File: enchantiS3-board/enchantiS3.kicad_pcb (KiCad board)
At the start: 4 copper layers, 55.9 x 25.4 mm, 59 parts, among them J1 USB_C_Receptacle_USB2.0, SW1 B3U-1000P, SW2 B3U-1000P, U1 USBLC6-2P6, U11 MAX17262REWL+T, U12 BQ25185DLHR, U13 ICM-42670-P, U2 MMC5633NJL, U4 NCP167AMX330TBG, U9 NCP167AMX330TBG

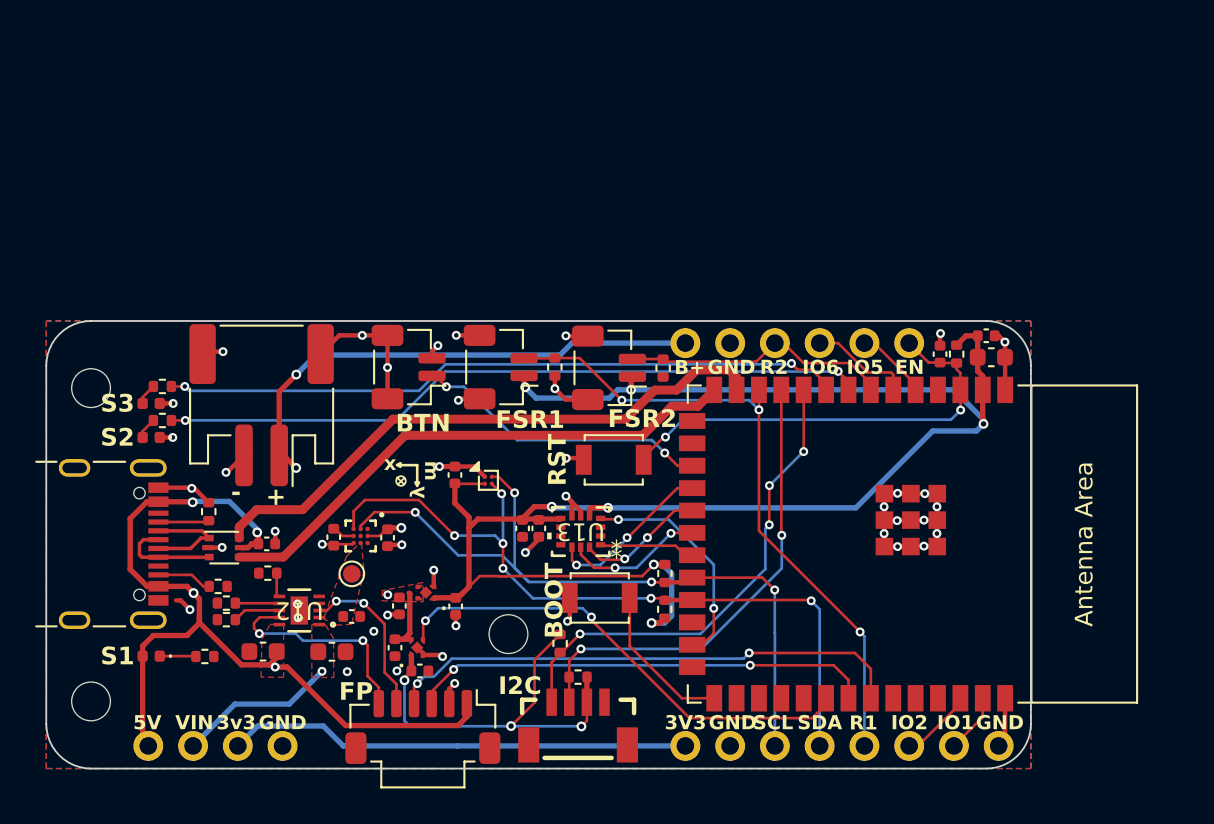
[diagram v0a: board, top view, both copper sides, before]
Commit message: revert tto two layer board, swap out magnetometer to mmc55983 and fuel gauge to MAX17260
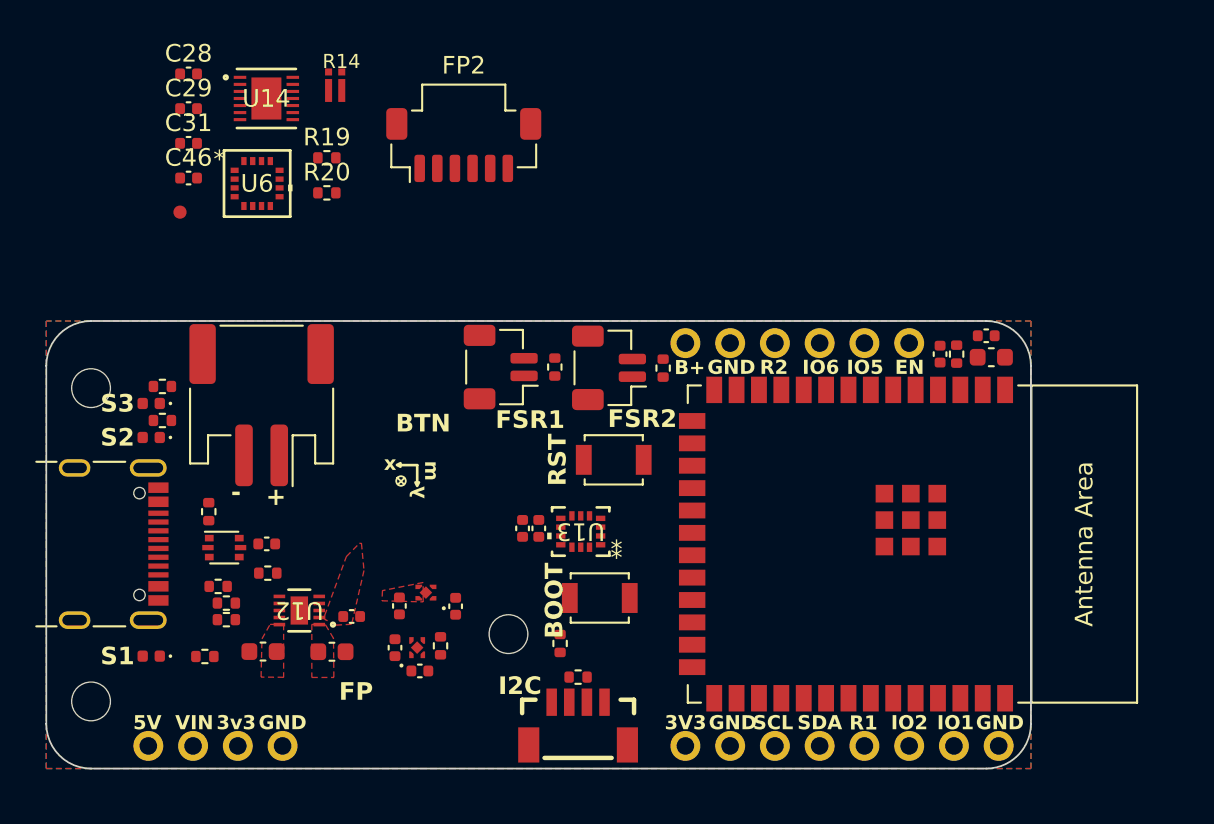
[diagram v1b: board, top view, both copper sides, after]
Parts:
- removed ANG2: CONN HEADER SMD 2POS 1MM, ENCHANTI_connectors:Molex_Pico-Clasp_2pin_Vertical
- removed C3: 220nF, Capacitor_SMD:C_0402_1005Metric
- removed C7: 0.1uF, Capacitor_SMD:C_0402_1005Metric
- removed C8: 0.47uF, Capacitor_SMD:C_0402_1005Metric
- removed FP1: CONN HEADER SMD 6POS 1MM, ENCHANTI_connectors:Molex_Pico-Clasp_501331-0607_1x06-1MP_P1.00mm_Vertical
- removed R4, R9: 2k2, Resistor_SMD:R_0402_1005Metric
- removed TP1: TestPoint, TestPoint:TestPoint_Pad_D1.0mm
- removed U11: MAX17262REWL+T, ENCHANTI_battery-management:MAX17262
- removed U2: MMC5633NJL, Package_BGA:WLP-4_0.86x0.86mm_P0.4mm
- added C28: 1uF, Capacitor_SMD:C_0402_1005Metric, F.Cu at (100.8, 34.2)
- added C29: 10uF, Capacitor_SMD:C_0402_1005Metric, F.Cu at (100.8, 36.2)
- added C31: 0.1uF, Capacitor_SMD:C_0402_1005Metric, F.Cu at (100.8, 38.2)
- added C46: 0.47uF, Capacitor_SMD:C_0402_1005Metric, F.Cu at (100.8, 40.1)
- added FP2: CONN HEADER SMD 6POS 1MM, Connector_Molex:Molex_Pico-Clasp_501331-0607_1x06-1MP_P1.00mm_Vertical, F.Cu at (116.4, 38.3)
- added R14: 1mOhm, ENCHANTI_resistors:L4CC0306, F.Cu at (109.1, 34.9)
- added R19: 2k2, Resistor_SMD:R_0402_1005Metric, F.Cu at (108.6, 39.0)
- added R20: 2k2, Resistor_SMD:R_0402_1005Metric, F.Cu at (108.6, 41.0)
- added R22: 100k, Resistor_SMD:R_0402_1005Metric, F.Cu at (115.1, 66.7)
- added TP4: TestPoint, SparkFun-Connector:TestPoint-0.75mm, F.Cu at (100.3, 42.1)
- added U14: MAX17260SETD+T, ENCHANTI_battery-management:TDFN-14-EP-ADI, F.Cu at (105.2, 35.6)
- added U6: MMC5983MA, ENCHANTI_MEMS:MMC5983MA_MEM, F.Cu at (104.7, 40.5)
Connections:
- ANG1 pad 1: +3V3 -> 3V3_AUX
- ANG3 pad 1: +3V3 -> 3V3_AUX
- C17 pad 1: +3V3 -> 3V3_AUX
- C18 pad 1: +3V3 -> 3V3_AUX
- U13 pad 5: +3V3 -> 3V3_AUX
- U13 pad 8: +3V3 -> 3V3_AUX
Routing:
- net +3V3: track 132.4 -> 0.00 mm, vias 7 -> 0
- net GND: track 65.2 -> 0.00 mm, vias 44 -> 0
- net VUSB: track 48.2 -> 0.00 mm, vias 4 -> 0
- net /SDA: track 42.6 -> 0.00 mm, vias 6 -> 0
- net /SCL: track 42.0 -> 0.00 mm, vias 4 -> 0
- net /BLUELED: track 40.3 -> 0.00 mm, vias 2 -> 0
- net /ORANGELED: track 38.7 -> 0.00 mm, vias 2 -> 0
- net /FSR1: track 37.2 -> 0.00 mm, vias 3 -> 0
- net /USBD-: track 33.4 -> 0.00 mm
- net +BATT: track 31.2 -> 0.00 mm, vias 3 -> 0
- net /USBD+: track 30.9 -> 0.00 mm
- net /LED2: track 29.7 -> 0.00 mm, vias 2 -> 0
- net /SCL2: track 27.7 -> 0.00 mm, vias 4 -> 0
- net /LDO_EN: track 27.6 -> 0.00 mm, vias 2 -> 0
- net /SDA2: track 26.7 -> 0.00 mm, vias 2 -> 0
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- removed copper zone on In2.Cu, net +3V3
- removed copper zone on In2.Cu, net +BATT
- removed copper zone on In1.Cu, net GND
- removed copper zone on In2.Cu, net GND
- removed copper zone on In2.Cu, net SYS
- removed copper zone on In2.Cu, net VUSB
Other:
- copper layers 4 -> 2
- rule pad_to_mask_clearance: 0.0508 -> 0
- board text removed: "1.8V"
- board text removed: "2 pin JST-PH Vertical Header"
- board text removed: "2 pin JST-SH Vertical Header"
- board text removed: "3.3V"
- board text removed: "4 pin JST-SH Vertical Header"
- board text removed: "BAT+"
- board text removed: "Boot Button"
- board text removed: "ESP32-S3 WROOM 2"
- board text removed: "Fuel Gauge"
- board text removed: "ICM20948"
- board text removed: "Indicator LEDs (RED)"
- board text removed: "MCP73871"
- board text removed: "NCP167AMX 180TBG"
- board text removed: "NCP167AMX 330TBG"
- board text removed: "Neopixel"
- board text removed: "Ohmite LVK12 Shunt Resistor"
- board text removed: "Reset Button"
- board text removed: "SYS"
- board text removed: "USB C Receptacle"
- board text removed: "USBLC6-LP6"

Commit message: Switched to using multi sheet schematic, added NPM1300 to handle power management and WiFi, finished initial PCB layout and routing
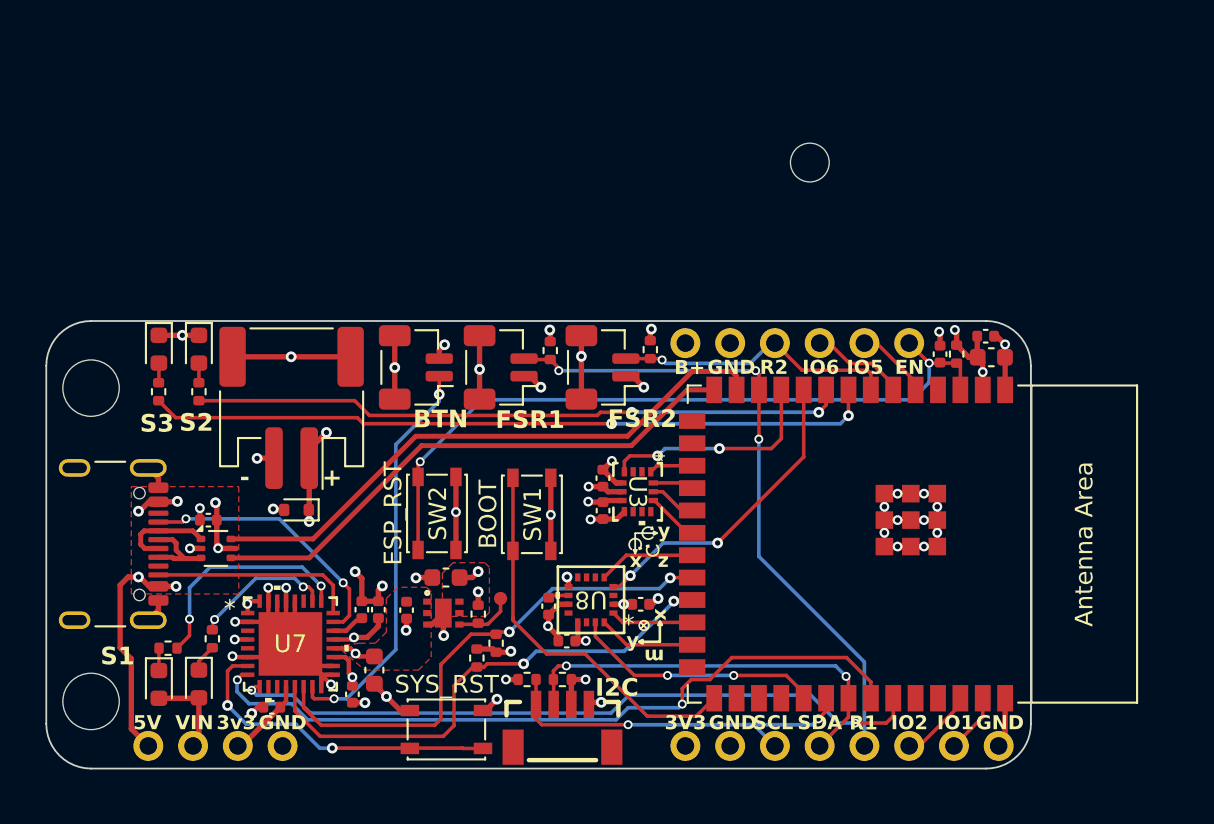
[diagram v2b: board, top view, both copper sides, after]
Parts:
- removed BT1: JST-PH-1x02-2.000mm, Connector_JST:JST_PH_S2B-PH-SM4-TB_1x02-1MP_P2.00mm_Horizontal
- removed C12, C17, C22, C28: 1uF, Capacitor_SMD:C_0402_1005Metric
- removed C21, C23: 10uF, Capacitor_SMD:C_0603_1608Metric
- removed C29: 10uF, Capacitor_SMD:C_0402_1005Metric
- removed C31: 0.1uF, Capacitor_SMD:C_0402_1005Metric
- removed C46: 0.47uF, Capacitor_SMD:C_0402_1005Metric
- removed CHARGLED1: S1, LED_SMD:LED_0402_1005Metric
- removed FP2: CONN HEADER SMD 6POS 1MM, Connector_Molex:Molex_Pico-Clasp_501331-0607_1x06-1MP_P1.00mm_Vertical
- removed the G*** at (103.9, 51.2)
- removed R11: 13k, Resistor_SMD:R_0402_1005Metric
- removed R13, R19, R20: 2k2, Resistor_SMD:R_0402_1005Metric
- removed R14: 1mOhm, ENCHANTI_resistors:L4CC0306
- removed R15: 0.3k, Resistor_SMD:R_0402_1005Metric
- removed R21: 10k, Resistor_SMD:R_0402_1005Metric
- removed R22: 100k, Resistor_SMD:R_0402_1005Metric
- removed STATLED1: WIFISTATUS, LED_SMD:LED_0402_1005Metric
- removed STATLED2: GENERAL STATUS, LED_SMD:LED_0402_1005Metric
- removed TP4: TestPoint, SparkFun-Connector:TestPoint-0.75mm
- removed U12: BQ25185DLHR, ENCHANTI_battery-management:WSON10_DLH_TEX
- removed U13: ICM-42670-P, ENCHANTI_MEMS:LGA14_2P5X3X0P91_TDK
- removed U14: MAX17260SETD+T, ENCHANTI_battery-management:TDFN-14-EP-ADI
- removed U4, U9: NCP167AMX330TBG, ENCHANTI_regulators:XDFN4_1X1_711AJ_ONS
- removed U6: MMC5983MA, ENCHANTI_MEMS:MMC5983MA_MEM
- added ANG2: CONN HEADER SMD 2POS 1MM, ENCHANTI_connectors:Molex_Pico-Clasp_2pin_Vertical, F.Cu at (113.7, 50.9)
- added BAT1: JST_SMD_2.0, ENCHANTI_connectors:Battery_JST_2pin, F.Cu at (106.5, 53.2)
- added C1: 1uF, Capacitor_SMD:C_0402_1005Metric, F.Cu at (111.6, 64.6)
- added C10: 10uF, Capacitor_SMD:C_0603_1608Metric, F.Cu at (115.4, 62.8)
- added C2: 0.1uF, Capacitor_SMD:C_0402_1005Metric, F.Cu at (146.0, 49.1)
- added C20: 0.1uF, Capacitor_SMD:C_0402_1005Metric, F.Cu at (105.5, 70.2)
- added C3: 2.2uF, Capacitor_SMD:C_0402_1005Metric, F.Cu at (124.3, 59.0)
- added C6: 1uF, Capacitor_SMD:C_0402_1005Metric, F.Cu at (126.4, 64.3)
- added C7: 0.1uF, Capacitor_SMD:C_0402_1005Metric, F.Cu at (122.2, 66.4)
- added C8: 0.1uF, Capacitor_SMD:C_0402_1005Metric, F.Cu at (124.3, 57.2)
- added CHARGLED4: RED_LED, LED_SMD:LED_0603_1608Metric, F.Cu at (99.1, 68.9)
- added CHARGLED5: YELLOW_LED, LED_SMD:LED_0603_1608Metric, F.Cu at (101.4, 68.9)
- added D1: DZ2S051X0L, Diode_SMD:D_SOD-523, F.Cu at (106.9, 59.0)
- added LED1: Orange, LED_SMD:LED_0603_1608Metric, F.Cu at (101.4, 49.9)
- added LED2: Blue, LED_SMD:LED_0603_1608Metric, F.Cu at (99.1, 49.9)
- added R18: 2k, Resistor_SMD:R_0402_1005Metric, F.Cu at (102.1, 66.3)
- added R4: 2k2, Resistor_SMD:R_0402_1005Metric, F.Cu at (118.2, 66.5)
- added R9: 2k2, Resistor_SMD:R_0402_1005Metric, F.Cu at (122.0, 68.6)
- added SW3: SYS_RST, ENCHANTI_switches:SW_SPST_PTS810, F.Cu at (115.4, 71.4)
- added TP1: 0.75mm, SparkFun-Connector:TestPoint-0.75mm, F.Cu at (118.5, 64.0)
- added U2: NCP187, ENCHANTI_regulators:NCV8187_ONS, F.Cu at (115.2, 64.8)
- added U3: ICM-42670-P, ENCHANTI_MEMS:LGA14_2P5X3X0P91_TDK, F.Cu at (126.3, 58.0)
- added U7: NPM1300-QEAA-R7, ENCHANTI_battery-management:QFN32_5X5_NOR, F.Cu at (106.6, 66.6)
- added U8: MMC5983MA, ENCHANTI_MEMS:MMC5983MA_MEM, F.Cu at (123.6, 64.1)
- BOARDLAYOUT1: footprint pin-layout:board-layout -> ENCHANTI_enchanti-board-symbols:enchantiS3-layout
- C18: value 0.1uF -> 2.2uF
- C19: value 0.1uF -> 10uF
- C5: value 1uF -> 10uF; footprint Capacitor_SMD:C_0402_1005Metric -> Capacitor_SMD:C_0603_1608Metric
- G***: footprint logos:CIRMMT_logo -> ENCHANTI_enchanti-board-symbols:CIRMMT_logo
- G***: footprint logos:IDMIL_logo -> ENCHANTI_enchanti-board-symbols:IDMIL_logo
- H1, H2: footprint MountingHole:MountingHole_2.2mm_M2 -> MountingHole:MountingHole_3.2mm_M3_DIN965
- R1, R2: value 10k -> 1k
- R12: value 2k2 -> 2k
- R6: value 5k1 -> 10k
- R7: value 5k1 -> 2k2
- SW1: value B3U-1000P -> BOOT; footprint Button_Switch_SMD:SW_SPST_B3U-1000P -> ENCHANTI_switches:SW_SPST_PTS810
- SW2: value B3U-1000P -> ESP_RST; footprint Button_Switch_SMD:SW_SPST_B3U-1000P -> ENCHANTI_switches:SW_SPST_PTS810
- moved H3 31.8 mm to (136.0, 39.3)
- moved C19 29.2 mm to (121.2, 64.4), turned to -90 degrees
- moved R12 23.3 mm to (99.6, 66.8)
- moved R7 20.4 mm to (120.0, 68.6), turned to 180 degrees
- moved R3 15.4 mm to (117.1, 67.4), turned to 90 degrees
- moved R6 14.8 mm to (117.2, 64.9), turned to 90 degrees
- moved C18 13.5 mm to (110.1, 69.4)
- moved SW2 10.5 mm to (114.9, 59.2), turned to 90 degrees
- moved SW1 6.11 mm to (120.3, 59.2), turned to 90 degrees
- moved C15 3.58 mm to (101.9, 59.6), turned to 180 degrees
- moved C4 2.86 mm to (110.6, 64.6), turned to 90 degrees
- moved C5 2.58 mm to (111.3, 68.1), turned to -90 degrees
- moved R10 2.09 mm to (101.4, 52.3), turned to 90 degrees
- moved R8 1.65 mm to (99.1, 52.3), turned to 90 degrees
- moved R2 1.28 mm to (127.0, 49.9)
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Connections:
- net /BLUELED renamed /MCU/BLUELED
- net /D+ renamed /USB/D+
- net /D- renamed /USB/D-
- net /EN renamed /MCU/EN
- net /IO0 renamed /MCU/IO0
- net /IO1 renamed /MCU/IO1
- net /IO2 renamed /MCU/IO2
- net /IO5 renamed /MCU/IO5
- net /IO6 renamed /MCU/IO6
- net /ORANGELED renamed /MCU/ORANGELED
- net /RXD renamed /MCU/RXD
- net /TXD renamed /MCU/TXD
- net /USBD+ renamed /MCU/USBD+
- net /USBD- renamed /MCU/USBD-
- ANG1 pad 1: 3V3_AUX -> +3V3
- ANG1 pad 2: /FSR1 -> /MCU/FSR1
- ANG3 pad 1: 3V3_AUX -> +3V3
- ANG3 pad 2: /FSR2 -> /MCU/FSR2
- BOARDLAYOUT1 pad 1.3: /FSR2 -> /MCU/FSR2
- BOARDLAYOUT1 pad 2.3: /SCL -> /Peripherals/SCL2
- BOARDLAYOUT1 pad 2.4: /SDA -> /Peripherals/SDA2
- BOARDLAYOUT1 pad 2.5: /FSR1 -> /MCU/FSR1
- C18 pad 1: 3V3_AUX -> +BATT
- C19 pad 1: +3V3 -> Net-(U8-CAP)
- C4 pad 1: SYS -> /Power System/VBUSOUT
- C5 pad 1: 3V3_AUX -> SYS
- J1 pad A5: Net-(J1-CC1) -> /Power System/CC1
- J1 pad B5: Net-(J1-CC2) -> /Power System/CC2
- MCU1 pad 10: /SCL2 -> /MCU/MAG_CS
- MCU1 pad 11: /SDA2 -> /Motion Sensing/IMU_INT1
- MCU1 pad 12: /FSR1 -> /MCU/FSR1
- MCU1 pad 17: /BTN -> /MCU/IMU_CIPO
- MCU1 pad 18: /CS -> /MCU/IMU_COPI
- MCU1 pad 19: /COPI -> /MCU/IMU_SCLK
- MCU1 pad 20: /SCLK -> /MCU/IMU_CS
- MCU1 pad 21: /CIPO -> /MCU/MAG_CIPO
- MCU1 pad 22: /SCL -> /MCU/I2C_SCL_MAIN
- MCU1 pad 23: /SDA -> /MCU/I2C_SDA_MAIN
- MCU1 pad 24: /LED4 -> /MCU/MAG_SCLK
- MCU1 pad 25: /IMU_INT -> /MCU/MAG_COPI
- MCU1 pad 31: /BTN_FP -> /MCU/MAG_INT
- MCU1 pad 32: /LDO_EN -> /Peripherals/SCL2
- MCU1 pad 33: /LED1 -> /Peripherals/SDA2
- MCU1 pad 34: /LED2 -> /MCU/GPIO41
- MCU1 pad 35: /LED3 -> /MCU/GPIO42
- MCU1 pad 7: /FSR2 -> /MCU/FSR2
- R1 pad 1: /FSR1 -> GND
- R1 pad 2: GND -> /MCU/FSR1
- R12 pad 1: /SDA2 -> Net-(CHARGLED4-K)
- R12 pad 2: 3V3_AUX -> /Power System/LED0
- R2 pad 1: /FSR2 -> GND
- R2 pad 2: GND -> /MCU/FSR2
- R3 pad 1: Net-(CHARGLED1-K) -> /MCU/I2C_SDA_MAIN
- R3 pad 2: GND -> +3V3
- R6 pad 1: GND -> /Power System/PG
- R6 pad 2: Net-(J1-CC2) -> +3V3
- R7 pad 1: GND -> /Peripherals/SCL2
- R7 pad 2: Net-(J1-CC1) -> +3V3
- TOUCH1 pad 2: 3V3_AUX -> +3V3
- TOUCH1 pad 3: /SDA2 -> /Peripherals/SDA2
- TOUCH1 pad 4: /SCL2 -> /Peripherals/SCL2
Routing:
- net GND: track 0.00 -> 109.1 mm, vias 0 -> 46
- net +3V3: track 0.00 -> 51.1 mm, vias 0 -> 13
- net +BATT: track 0.00 -> 43.4 mm, vias 0 -> 3
- net /MCU/EN: track 0.00 -> 41.7 mm, vias 0 -> 2
- net /MCU/GPIO41: track 0.00 -> 41.5 mm, vias 0 -> 2
- net /MCU/BLUELED: track 0.00 -> 41.3 mm, vias 0 -> 2
- net /MCU/GPIO42: track 0.00 -> 39.7 mm, vias 0 -> 2
- net /MCU/FSR1: track 0.00 -> 37.4 mm, vias 0 -> 3
- net /MCU/ORANGELED: track 0.00 -> 37.0 mm, vias 0 -> 2
- net /MCU/USBD-: track 0.00 -> 33.5 mm
- net VUSB: track 0.00 -> 33.0 mm, vias 0 -> 7
- net /MCU/USBD+: track 0.00 -> 31.4 mm
- net /MCU/I2C_SCL_MAIN: track 0.00 -> 29.1 mm, vias 0 -> 2
- net /MCU/I2C_SDA_MAIN: track 0.00 -> 29.1 mm, vias 0 -> 2
- net SYS: track 0.00 -> 26.2 mm, vias 0 -> 3
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- added copper zone on F.Cu, net +3V3
- added copper zone on In2.Cu, net +3V3
- added copper zone on In1.Cu, net GND
- added copper zone on In2.Cu, net GND
- added copper zone on In2.Cu, net VUSB
- removed copper zone on F.Cu, net CHRG+
- removed copper zone on B.Cu, net GND
- removed copper zone on F.Cu, net GND
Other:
- copper layers 2 -> 4
- board text removed: "+"
- board text removed: "-"
- board text removed: "BOOT"
- board text removed: "FP"
- board text removed: "MIMU ORIENTATION"
- board text removed: "RST"
- board text removed: "a"
- board text removed: "g"
- board text removed: "n"

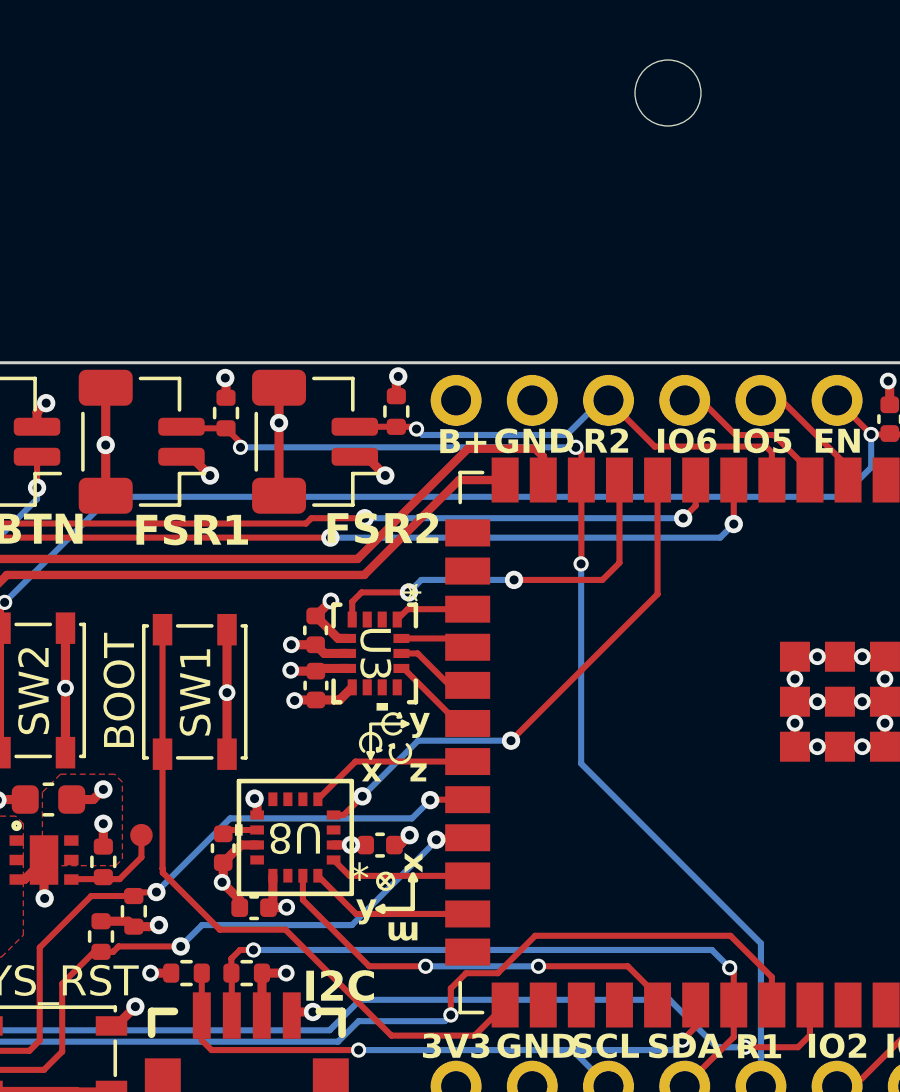
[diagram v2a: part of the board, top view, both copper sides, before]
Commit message: Fixed BOM errors, removed unused Mounting Hole, added rev4 BOM
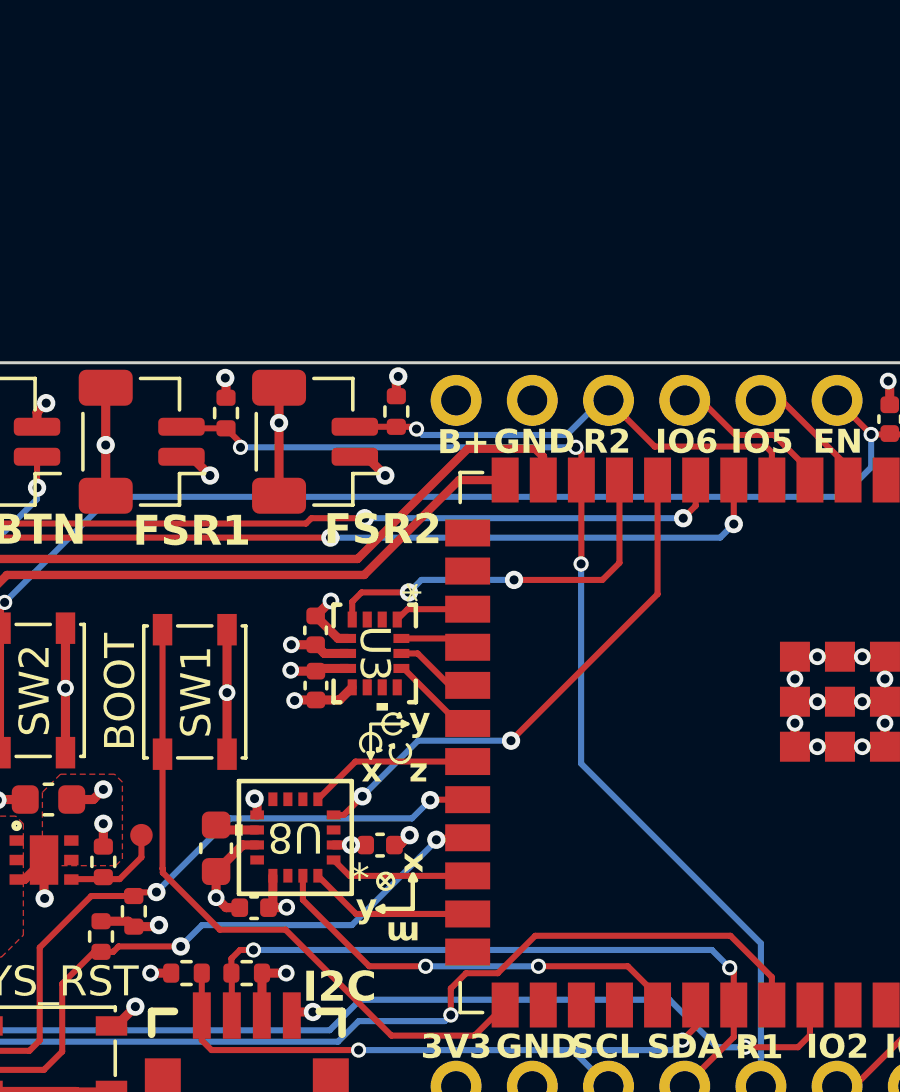
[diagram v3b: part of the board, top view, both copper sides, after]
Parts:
- removed H3: MountingHole, MountingHole:MountingHole_2.2mm_M2
- C19: footprint Capacitor_SMD:C_0402_1005Metric -> Capacitor_SMD:C_0603_1608Metric
- moved C19 0.24 mm to (121.0, 64.4)
